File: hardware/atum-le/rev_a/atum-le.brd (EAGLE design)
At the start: 18.8 x 19.6 mm, 41 parts, among them J2 SH_MALE_2/1MM, J3 ATUM-HEADER, U1 CC2538, U2 FM25LBTDFN-8, U3 RV-3049-C3, U4 TPS62740, X1 EPSON-FA-128, X2 ABS05-32.768KHZ-T

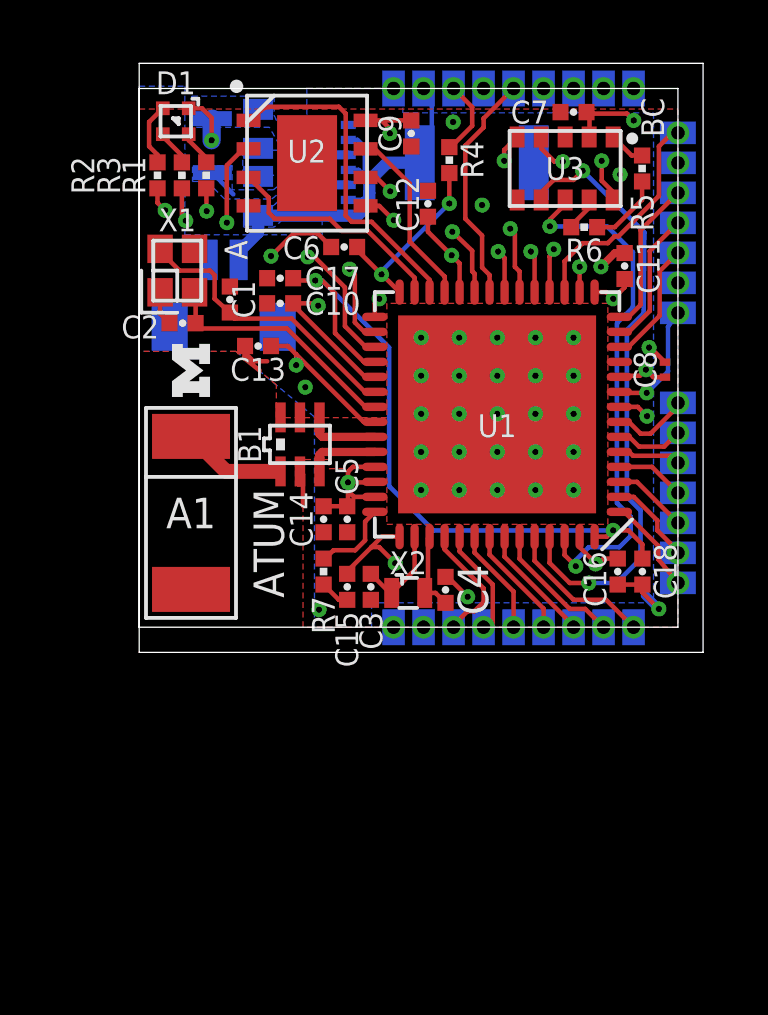
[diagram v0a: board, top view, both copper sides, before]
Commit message: improved signal routing and mapping
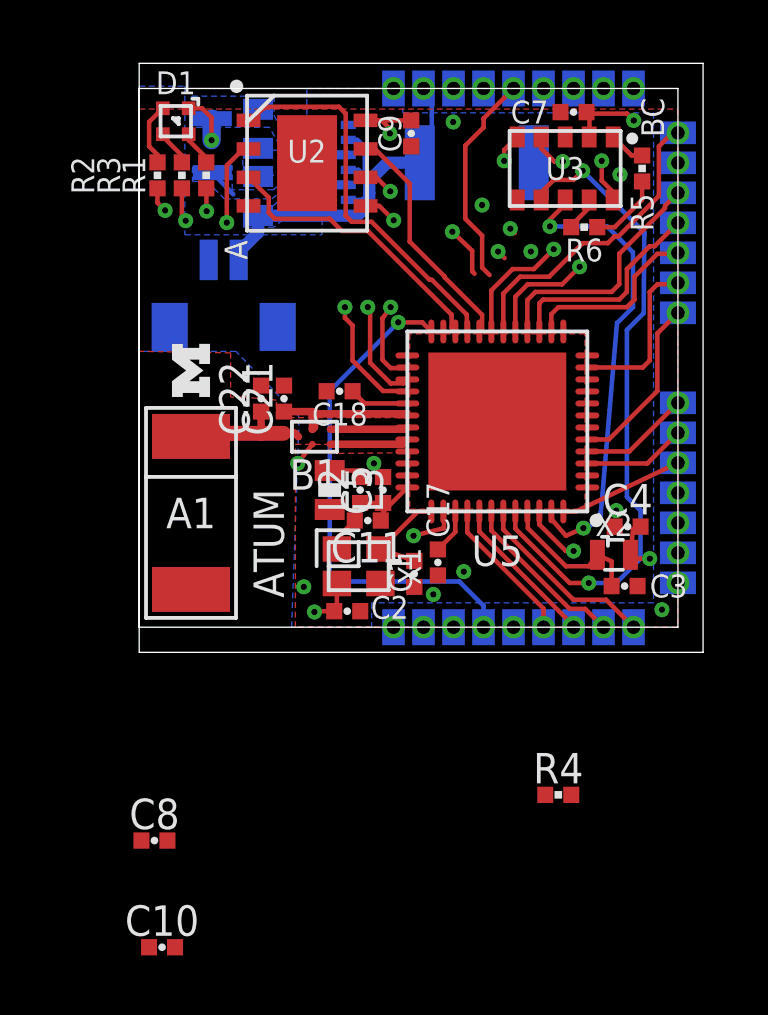
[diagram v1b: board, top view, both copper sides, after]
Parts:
- removed C12, C13, C14, C15: 0.1uF, passives:0402_CAP
- removed C16: 1uF, passives:0402_CAP
- removed C6: 1nF, passives:0402_CAP
- removed R7: 56k, passives:0402_RES
- removed U1: CC2538, chips:S-PVQFN-N56
- added C21: 2.2nF, passives:0402_CAP
- added C22: 0.8pF, passives:0402_CAP
- added L2: (no value), passives:0402_CAP
- added L3: (no value), passives:0603_CAP
- added U5: NRF51822QF, chips:QFN-48-6MM
- B1: value 2450BM15A0002 -> BAL-NRF01D3; device chips:2450BM -> chips:BAL-NRF01D3
- C10: value 0.1uF -> 4.7uF
- C11: value 0.1uF -> 1uF
- C17: value 1uF -> 1nF
- C18: value 1uF -> 47nF
- C5: value 220pF -> 1nF
- C8: device rcl:C0201 -> passives:0402_CAP
- R4: value 2.2k -> 12k
- moved C8 23.2 mm to (0.51, -7.11), turned to 0 degrees
- moved C10 21.8 mm to (0.76, -10.7), turned to 0 degrees
- moved R4 21.5 mm to (14.0, -5.59), turned to 0 degrees
- moved C11 12.1 mm to (7.62, 3.56), turned to 180 degrees
- moved C18 11.7 mm to (6.68, 7.87), turned to 180 degrees
- moved X1 11.6 mm to (7.32, 2.03), turned to 180 degrees
- moved C2 11.1 mm to (6.93, 0.53), turned to 0 degrees
- moved C1 11.0 mm to (9.17, 1.78), turned to 270 degrees
- moved C17 10.8 mm to (9.96, 2.16), turned to 270 degrees
- moved C3 8.46 mm to (16.2, 1.37), turned to 0 degrees
- moved X2 6.97 mm to (15.8, 2.41)
- moved C4 6.43 mm to (16.3, 3.35), turned to 180 degrees
- moved C5 1.54 mm to (8.13, 4.57), turned to 90 degrees
- moved B1 0.55 mm to (5.84, 6.35)
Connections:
- removed net !RESET: J3.30, J3.30B, R4.1
- removed net ADC3: J3.25, J3.25B, U1.19
- removed net ADC4: J3.26, J3.26B, U1.20
- removed net ADC5: J3.27, J3.27B, U1.21
- removed net ADC6: J3.28, J3.28B, U1.22
- removed net ADC7: J3.29, J3.29B, U1.23
- removed net DGND_USB: J3.10, J3.10B, U1.1
- removed net DVDD_USB: J3.13, J3.13B, U1.4
- removed net N$1: C6.1, R4.2, U1.28
- removed net N$8: R7.1, U1.42
- removed net RF_N: B1.3, U1.38
- removed net RF_P: B1.4, U1.37
- removed net TCK: J3.4, J3.4B, U1.47
- removed net TDO: J3.5, J3.5B, U1.48
- removed net TMS: J3.3, J3.3B, U1.46
- removed net USB_N: J3.12, J3.12B, U1.3
- removed net USB_P: J3.11, J3.11B, U1.2
- new net AIN2: J3.11, J3.11B
- new net AIN3: J3.25, J3.25B, U5.6
- new net AIN4: J3.26, J3.26B, U5.7
- new net AIN5: J3.27, J3.27B, U5.8
- new net AIN6: J3.28, J3.28B, U5.9
- new net AIN7: J3.29, J3.29B, U5.10
- new net AREF0: J3.10, J3.10B
- new net N$17: C17.1, U5.39
- new net N$18: B1.ANT1, U5.31
- new net N$19: B1.ANT2, U5.32
- new net N$20: B1.VCC, C21.1, U5.30
- new net N$36: C11.1, C5.1, L2.1, U5.35, U5.36
- new net N$37: L2.2, L3.1
- new net N$38: L3.2, U5.2
- new net N$43: J3.13, J3.13B
- new net SWDCLK: J3.4, J3.4B, R4.2, U5.24
- new net SWDIO/!RESET: J3.5, J3.5B, U5.23
- net !FRAM_CS: now also U5.21; no longer U1.26
- net !FRAM_HOLD: now also U5.20; no longer U1.25
- net !FRAM_WP: now also U5.22; no longer U1.27
- net !RTC_INT: now also U5.44; no longer U1.53
- net ANTENNA: now also B1.SE, C22.1; no longer B1.1
- net B3: now also U5.43; no longer U1.52
- net B4: now also U5.42; no longer U1.51
- net B5: now also U5.41; no longer U1.50
- net B6: now also U5.40; no longer U1.49
- net BOOTLOADER_CTRL: now also U5.19; no longer U1.18
- net BOOTLOADER_RX: now also U5.17; no longer U1.16
- net BOOTLOADER_TX: now also U5.18; no longer U1.17
- net C0: now also U5.16; no longer U1.14
- net C1: now also U5.15; no longer U1.13
- net C2: now also U5.14; no longer U1.12
- net C3: now also U5.25; no longer U1.11
- net GND: now also B1.GND, C21.2, C22.2, R4.1; no longer B1.2, B1.5, B1.6, C12.2, C13.2, C14.2, C15.2, C16.2, C6.2, R7.2, U1.VSS_QFN
- net I2C_SCL: now also U5.5; no longer U1.9
- net I2C_SDA: now also U5.11; no longer U1.8
- net LED_BLUE: now also U5.27; no longer U1.30
- net LED_GREEN: now also U5.28; no longer U1.31
- net LED_RED: now also U5.26; no longer U1.29
- net N$10: now also U5.38; no longer U1.35
- net N$13: now also U5.46; no longer U1.45
- net N$15: now also U5.29; no longer C17.1, U1.32, U1.56
- net N$6: now also U5.45; no longer U1.44
- net N$9: now also U5.37; no longer U1.34
- net RTC_CE: now also U5.47; no longer U1.54
- net SPI_MISO: now also U5.48; no longer U1.5
- net SPI_MOSI: now also U5.3; no longer U1.6
- net SPI_SCK: now also U5.4; no longer U1.7
- net VCC: now also U5.1, U5.12; no longer C11.1, C12.1, C13.1, C14.1, C15.1, C16.1, C5.1, U1.10, U1.15, U1.24, U1.33, U1.36, U1.39, U1.40, U1.41, U1.43, U1.55
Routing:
- net VCC: track 41.8 -> 9.59 mm, vias 11 -> 3
- net N$15: track 23.2 -> 1.99 mm, vias 2 -> 0
- net SWDCLK: track 0.00 -> 16.8 mm, vias 0 -> 1
- net GND: track 19.6 -> 8.23 mm, vias 35 -> 10
- net ADC3: track 8.29 -> 0.00 mm, vias 1 -> 0
- net ADC7: track 8.10 -> 0.00 mm, vias 1 -> 0
- net ADC5: track 7.95 -> 0.00 mm, vias 1 -> 0
- net ADC4: track 7.79 -> 0.00 mm, vias 1 -> 0
- net ADC6: track 7.79 -> 0.00 mm
- net AIN7: track 0.00 -> 7.49 mm, vias 0 -> 1
- net AIN6: track 0.00 -> 7.22 mm
- net AIN3: track 0.00 -> 7.06 mm, vias 0 -> 1
- net AIN5: track 0.00 -> 6.81 mm, vias 0 -> 1
- net N$1: track 6.40 -> 0.00 mm, vias 2 -> 0
- net N$9: track 9.67 -> 3.41 mm
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
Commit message: finished up schematic and did more routing
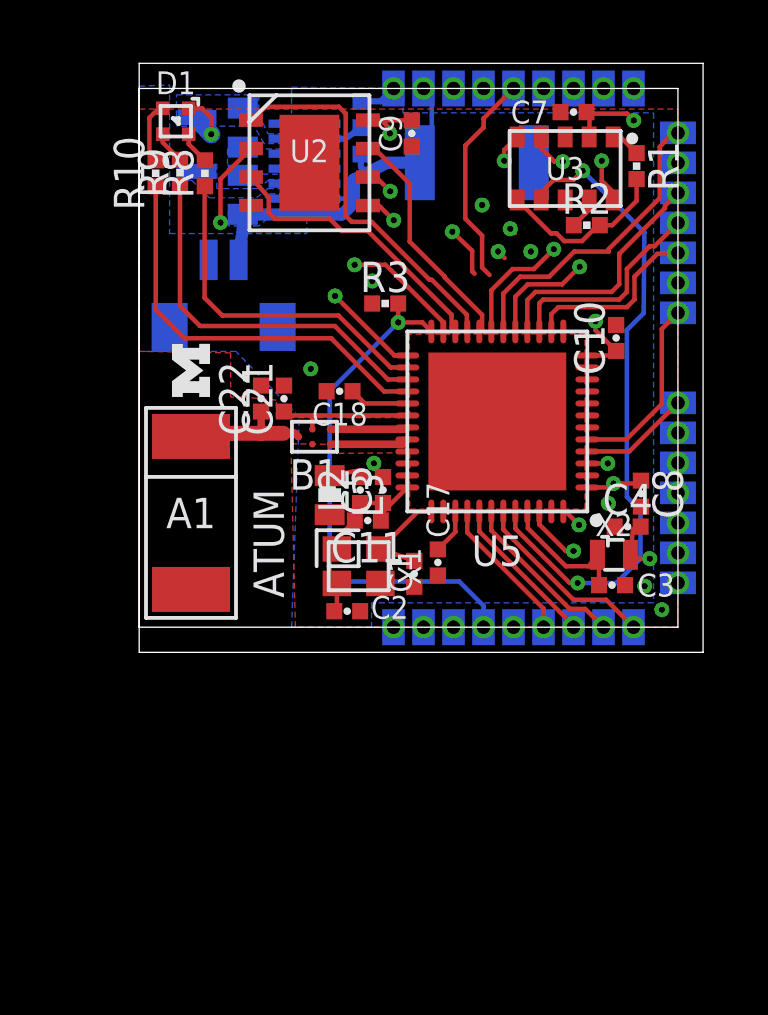
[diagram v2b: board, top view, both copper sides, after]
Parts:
- removed R4: 12k, passives:0402_RES
- removed R5, R6: 10k, passives:0402_RES
- added R10, R8, R9: 1k, passives:0402_RES
- added U$1: RES_SWITCH, switches:RES_SWITCH
- R1, R2: value 1k -> 10k
- R3: value 1k -> 12k
- moved C10 25.3 mm to (15.9, 9.64), turned to 90 degrees
- moved C8 19.9 mm to (16.7, 4.45), turned to 270 degrees
- moved R2 14.4 mm to (14.9, 13.4), turned to 0 degrees
- moved R1 14.3 mm to (16.6, 15.4)
- moved R3 8.01 mm to (8.20, 10.8), turned to 0 degrees
- moved C19 0.51 mm to (3.45, 14.4)
- moved C20 0.51 mm to (3.45, 16.7)
- moved L1 0.51 mm to (1.93, 16.1)
- moved U4 0.51 mm to (5.51, 15.5)
- moved C3 0.42 mm to (15.8, 1.40)
- moved L3 0.17 mm to (6.35, 4.40)
- moved U2 0.08 mm to (5.68, 15.5)
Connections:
- net B3 renamed P24
- net B4 renamed P23
- net B5 renamed P22
- net B6 renamed P21
- net C0 renamed P10
- net C1 renamed P09
- net C2 renamed P08
- removed net AIN2: J3.11, J3.11B
- removed net AREF0: J3.10, J3.10B
- removed net C3: U5.25
- removed net N$43: J3.13, J3.13B
- removed net UNUSED1: J3.2, J3.2B
- new net N$1: J3.30, J3.30B
- new net N$8: U$1.C, U4.8, U4.9
- new net P17: J3.2, J3.2B, U5.25
- net BATTERY: now also U$1.B; no longer U4.10, U4.8
- net GND: now also R1.2, R2.2, R3.1, U$1.A, U4.10; no longer R4.1, R5.1, R6.1, U4.9
- net LED_BLUE: now also R9.1; no longer R3.2
- net LED_GREEN: now also R10.1; no longer R2.2
- net LED_RED: now also R8.1; no longer R1.2
- net N$11: now also R10.2; no longer R2.1
- net N$12: now also R9.2; no longer R3.1
- net N$14: now also R2.1; no longer R6.2
- net N$16: now also R1.1; no longer R5.2
- net N$7: now also R8.2; no longer R1.1
- net SWDCLK: now also R3.2; no longer R4.2
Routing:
- net SPI_MISO: track 38.4 -> 19.0 mm, vias 2 -> 3
- net SWDIO/!RESET: track 0.00 -> 19.0 mm, vias 0 -> 1
- net P17: track 0.00 -> 16.5 mm, vias 0 -> 1
- net RTC_CE: track 15.9 -> 0.00 mm, vias 2 -> 0
- net N$10: track 7.60 -> 0.96 mm, vias 2 -> 0
- net I2C_SDA: track 10.4 -> 4.87 mm
- net GND: track 8.23 -> 11.2 mm, vias 10 -> 7
- net VCC: track 9.59 -> 11.4 mm, vias 3 -> 5
- net BATTERY: track 14.4 -> 12.8 mm
- net N$8: track 0.00 -> 1.55 mm
- net SPI_SCK: track 28.2 -> 27.0 mm
- net LED_RED: track 12.5 -> 11.4 mm, vias 2 -> 0
- net N$5: track 1.01 -> 0.00 mm
- net SWDCLK: track 16.8 -> 17.5 mm
- net SPI_MOSI: track 29.7 -> 29.1 mm, vias 2 -> 3
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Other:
- board text removed: "A"
- board text removed: "BC"

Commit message: added jtag, board routed but not DRCd
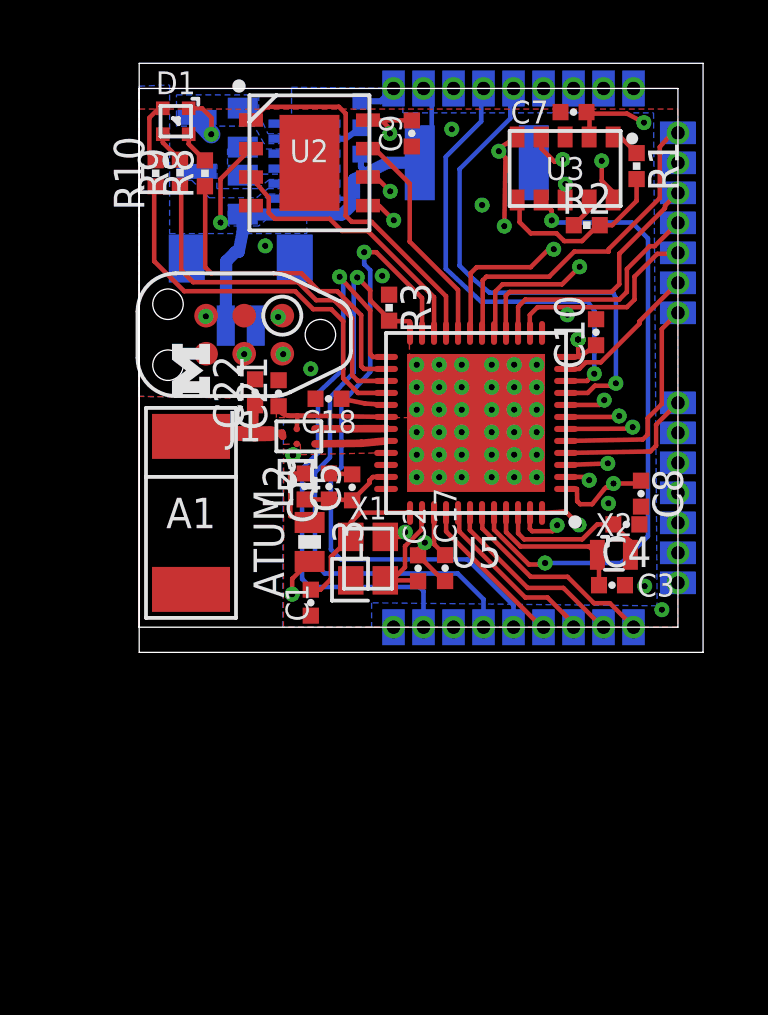
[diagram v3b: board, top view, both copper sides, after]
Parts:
- added J1: TC2030-JLINK-NL, connector:TC2030-IDC-NL
- moved C1 3.58 mm to (5.72, 0.82)
- moved C2 2.76 mm to (9.30, 1.96), turned to 90 degrees
- moved J2 2.46 mm to (3.38, 9.96), turned to 0 degrees
- moved L2 1.85 mm to (5.52, 4.69)
- moved C11 1.72 mm to (6.33, 4.69), turned to 90 degrees
- moved L3 1.70 mm to (5.68, 2.84)
- moved C5 1.03 mm to (7.10, 4.66)
- moved U5 0.71 mm to (11.2, 6.81)
- moved C10 0.70 mm to (15.2, 9.83)
- moved B1 0.52 mm to (5.32, 6.36)
- moved C18 0.45 mm to (6.31, 7.62)
- moved X1 0.40 mm to (7.63, 2.29), turned to 270 degrees
- moved C17 0.31 mm to (10.2, 1.97)
- moved C22 0.29 mm to (3.86, 7.83)
- moved C21 0.25 mm to (4.65, 7.80)
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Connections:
- net GND: now also J1.5
- net SWDCLK: now also J1.4
- net SWDIO/!RESET: now also J1.2
- net VCC: now also J1.1
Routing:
- net RTC_CE: track 0.00 -> 18.7 mm, vias 0 -> 2
- net N$38: track 0.00 -> 15.9 mm, vias 0 -> 2
- net SPI_MISO: track 19.0 -> 33.4 mm, vias 3 -> 4
- net AIN6: track 7.22 -> 17.0 mm, vias 0 -> 1
- net SWDIO/!RESET: track 19.0 -> 28.1 mm, vias 1 -> 2
- net SWDCLK: track 17.5 -> 25.9 mm, vias 1 -> 2
- net AIN4: track 5.76 -> 14.1 mm
- net AIN7: track 7.49 -> 15.2 mm
- net AIN3: track 7.06 -> 14.4 mm
- net AIN5: track 6.81 -> 13.9 mm
- net P17: track 16.5 -> 19.7 mm
- net N$10: track 0.96 -> 3.99 mm
- net GND: track 11.2 -> 13.8 mm, vias 7 -> 50
- net BATTERY: track 12.8 -> 15.3 mm
- net VCC: track 11.4 -> 13.5 mm, vias 5 -> 7
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
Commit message: fixed all drc errors
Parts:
- moved J1 0.97 mm to (2.53, 9.68)
- moved C2 0.88 mm to (8.95, 1.15), turned to 0 degrees
- moved L3 0.69 mm to (4.99, 2.78)
- moved J2 0.66 mm to (2.72, 10.0)
- moved B1 0.65 mm to (4.67, 6.44)
- moved C3 0.65 mm to (16.4, 1.27)
- moved C10 0.65 mm to (15.0, 10.4), turned to 180 degrees
- moved X1 0.57 mm to (7.07, 2.38)
- moved X2 0.51 mm to (16.3, 2.22)
- moved C18 0.40 mm to (5.91, 7.62)
- moved C17 0.39 mm to (10.2, 1.58)
- moved C1 0.33 mm to (6.02, 0.68), turned to 0 degrees
- moved U$1 0.32 mm to (7.41, 16.3)
- moved C4 0.26 mm to (16.4, 3.20)
- moved A1 0.19 mm to (1.91, 3.86)
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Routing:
- net GND: track 13.8 -> 22.0 mm, vias 50 -> 49
- net SPI_MISO: track 33.4 -> 36.8 mm
- net SWDCLK: track 25.9 -> 29.0 mm
- net AIN6: track 17.0 -> 18.7 mm
- net SPI_SCK: track 28.2 -> 26.5 mm
- net AIN7: track 15.2 -> 16.7 mm
- net SPI_MOSI: track 29.8 -> 31.1 mm
- net P17: track 19.7 -> 20.9 mm
- net SWDIO/!RESET: track 28.1 -> 29.1 mm
- net N$9: track 5.10 -> 6.06 mm
- net VCC: track 13.5 -> 14.4 mm, vias 7 -> 6
- net ANTENNA: track 4.10 -> 3.26 mm
- net N$18: track 2.40 -> 3.23 mm
- net N$6: track 5.03 -> 5.81 mm
- net BOOTLOADER_TX: track 11.4 -> 12.1 mm
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
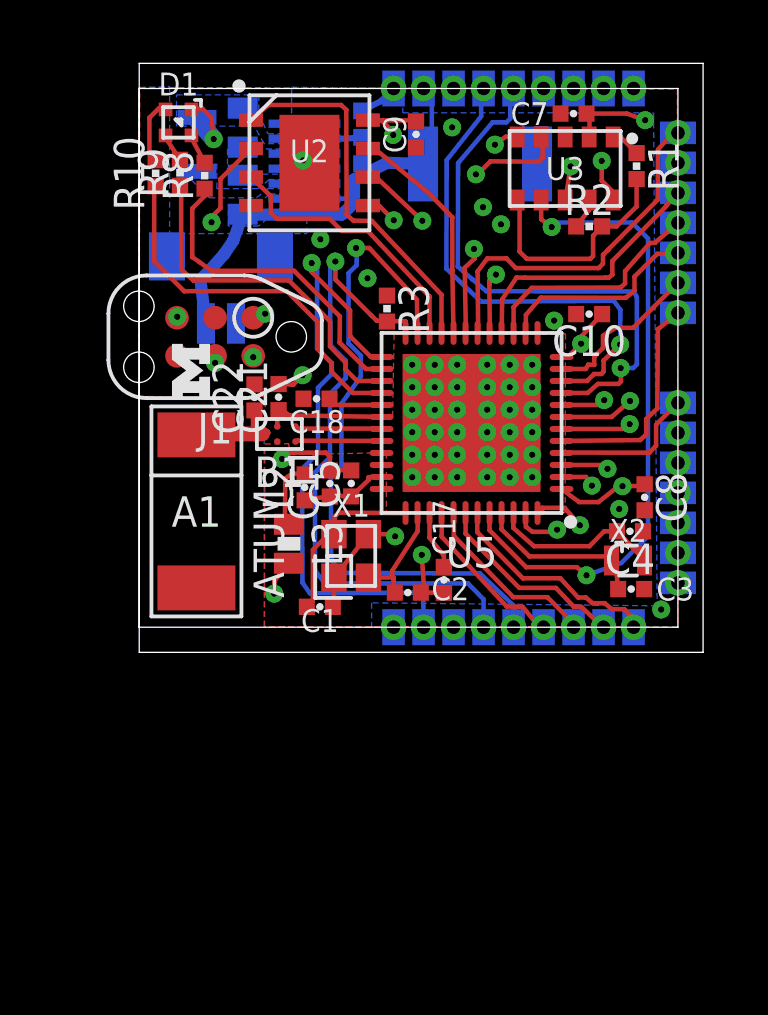
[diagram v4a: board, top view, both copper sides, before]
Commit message: fixed programming breakout, moved silk
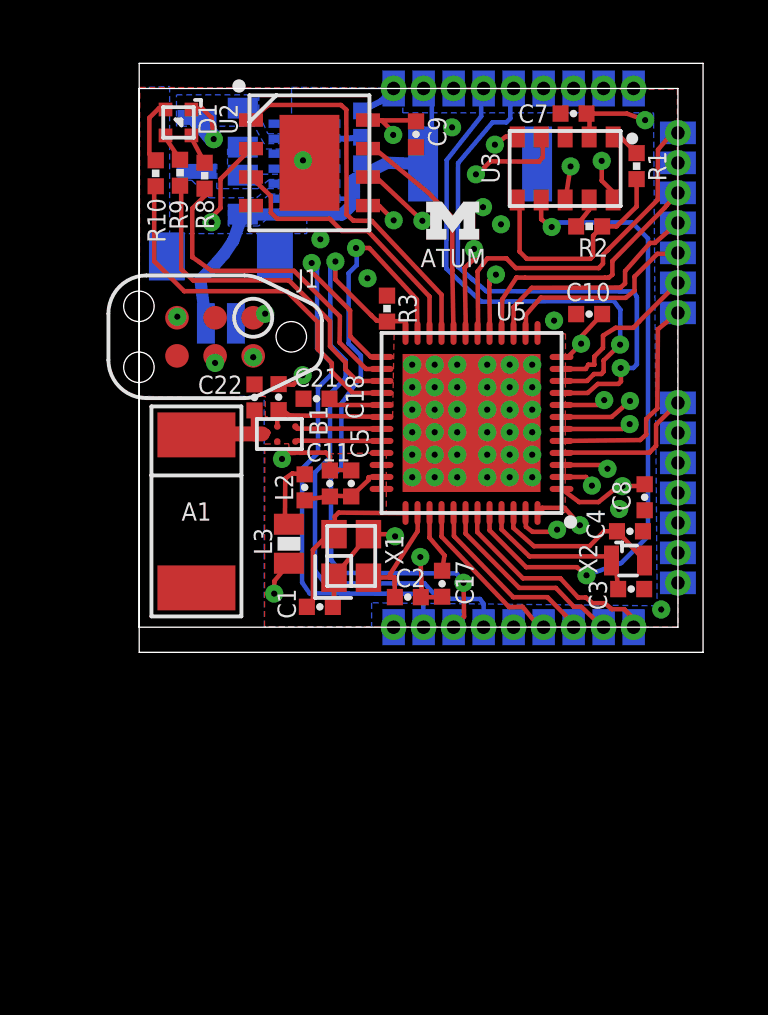
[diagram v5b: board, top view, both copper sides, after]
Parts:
- moved LOGO1 10.1 mm to (10.4, 13.6), turned to 0 degrees
- moved C2 0.15 mm to (8.95, 1.00)
- moved C17 0.14 mm to (10.1, 1.45)
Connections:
- removed net N$1: J3.30, J3.30B
- new net UNUSED1: J3.5, J3.5B
- new net UNUSED2: J3.10, J3.10B
- new net UNUSED3: J3.11, J3.11B
- new net UNUSED4: J3.12, J3.12B
- new net UNUSED5: J3.13, J3.13B
- net SWDIO/!RESET: now also J3.3, J3.30, J3.30B, J3.3B; no longer J3.5, J3.5B
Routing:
- net SWDIO/!RESET: track 29.1 -> 36.0 mm, vias 2 -> 3
- net N$38: track 16.5 -> 17.1 mm
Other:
- board text added: "2015/004/20"
- board text added: "Joshua Adkins Brad Campbell"
- board text removed: "2015/02/23"
- board text removed: "Brad Campbell"
